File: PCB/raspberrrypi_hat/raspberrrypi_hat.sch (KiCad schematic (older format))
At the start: 18 parts, among them J1 40HAT, J2 CONN_02X02, J3 CONN_01X02, Q1 DMG2305UX, Q2 DMMT5401, U1 CAT24C32

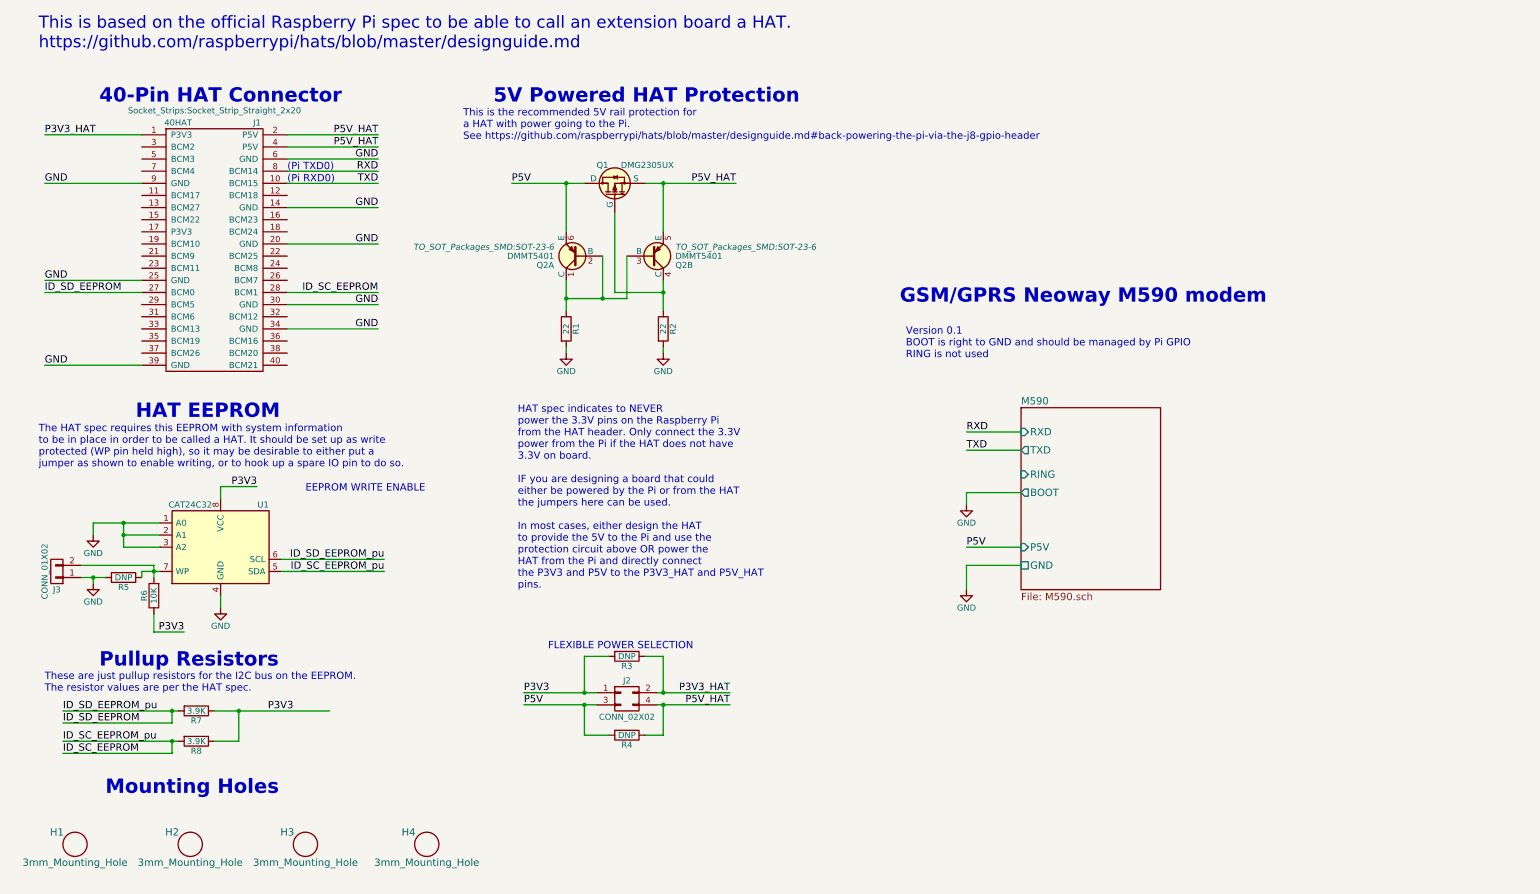
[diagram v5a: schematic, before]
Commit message: PCB: Change RPi header + add Micro SIM socket. Starting placement
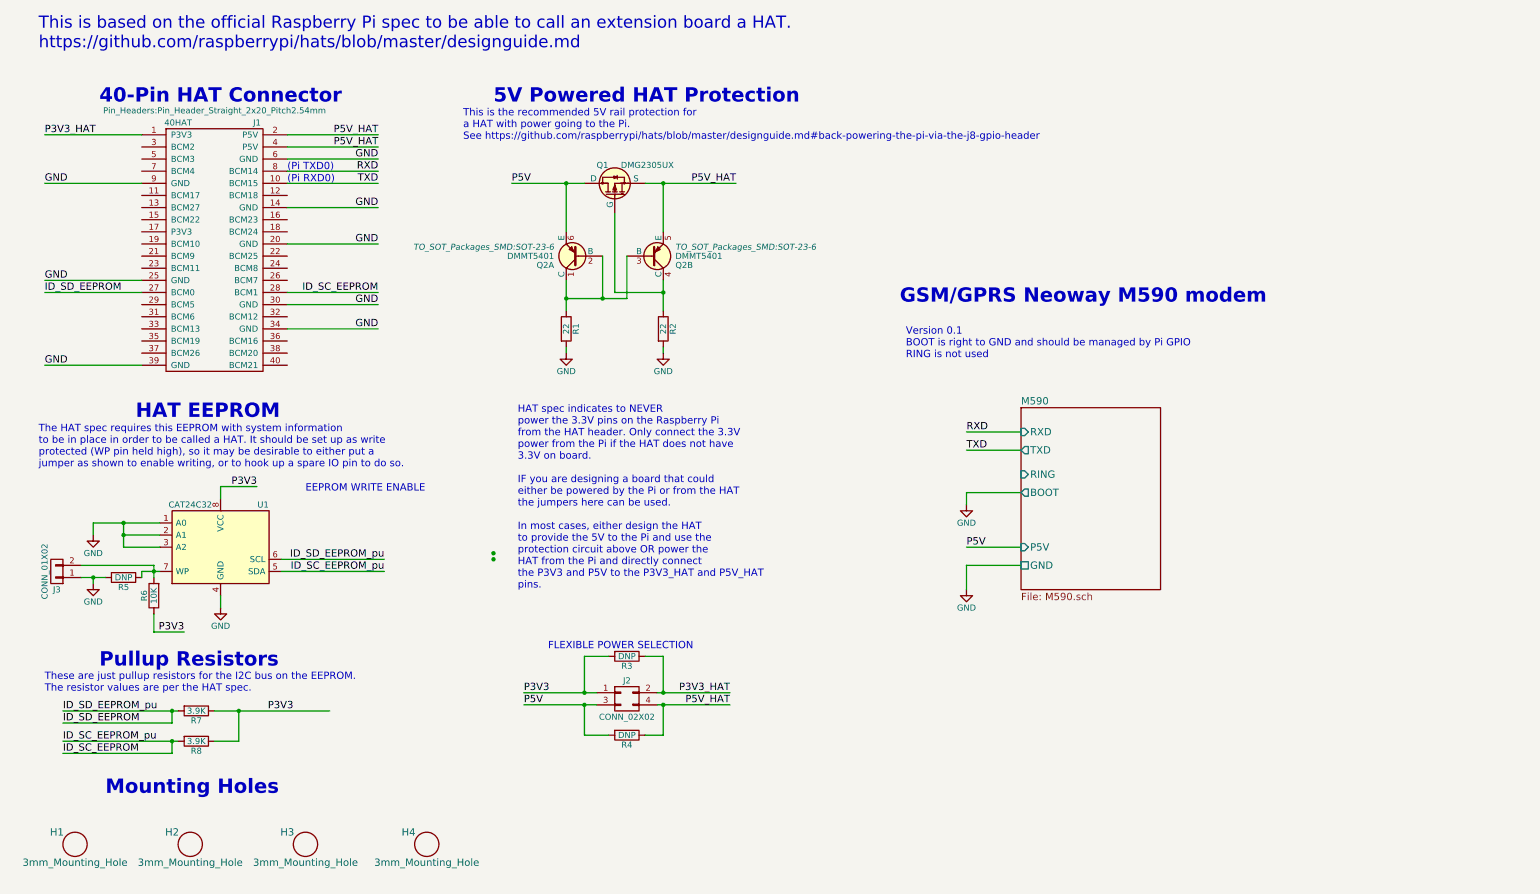
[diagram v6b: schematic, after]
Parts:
- J1: footprint Socket_Strips:Socket_Strip_Straight_2x20 -> Pin_Headers:Pin_Header_Straight_2x20_Pitch2.54mm
- J2: footprint Pin_Headers:Pin_Header_Straight_2x02 -> Pin_Headers:Pin_Header_Straight_2x02_Pitch2.54mm
- J3: footprint Pin_Headers:Pin_Header_Straight_1x02 -> Pin_Headers:Pin_Header_Straight_1x02_Pitch2.54mm
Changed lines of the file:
@@
 F 0 "J1" H 2450 1700 50  0000 C CNN
 F 1 "40HAT" H 1800 1700 50  0000 C CNN
-F 2 "Socket_Strips:Socket_Strip_Straight_2x20" H 2100 1800 50  0000 C CNN
+F 2 "Pin_Headers:Pin_Header_Straight_2x20_Pitch2.54mm" H 2100 1800 50  0000 C CNN
 F 3 "" H 1400 1600 50  0000 C CNN
 	1    2100 1600
@@
 F 0 "J2" H 5500 6400 50  0000 C CNN
 F 1 "CONN_02X02" H 5500 6100 50  0000 C CNN
-F 2 "Pin_Headers:Pin_Header_Straight_2x02" H 5500 5050 50  0001 C CNN
+F 2 "Pin_Headers:Pin_Header_Straight_2x02_Pitch2.54mm" H 5500 5050 50  0001 C CNN
 F 3 "" H 5500 5050 50  0000 C CNN
 	1    5500 6250
@@
 P5V
 Wire Wire Line
-	4650 6200 5150 6200
-Wire Wire Line
-	5150 6200 5250 6200
-Wire Wire Line
-	4650 6300 5150 6300
-Wire Wire Line
-	5150 6300 5250 6300
+	4650 6200 5250 6200
+Wire Wire Line
+	4650 6300 5250 6300
 Text Label 6350 6200 2    60   ~ 0
 P3V3_HAT
@@
 P5V_HAT
 Wire Wire Line
-	5750 6200 5800 6200
-Wire Wire Line
-	5800 6200 6350 6200
-Wire Wire Line
-	5750 6300 5800 6300
-Wire Wire Line
-	5800 6300 6350 6300
+	5750 6200 6350 6200
+Wire Wire Line
+	5750 6300 6350 6300
 Text Notes 4850 5850 0    60   ~ 0
 FLEXIBLE POWER SELECTION
@@
 P5V
 Wire Wire Line
-	4550 2000 5000 2000
-Wire Wire Line
-	5000 2000 5150 2000
+	4550 2000 5150 2000
 Text Notes 4400 1350 0    118  ~ 24
 5V Powered HAT Protection
@@
 $EndComp
 $Comp
-L GND #PWR1
+L GND #PWR01
 U 1 1 58E15A41
 P 5000 3400
-F 0 "#PWR1" H 5000 3150 50  0001 C CNN
+F 0 "#PWR01" H 5000 3150 50  0001 C CNN
 F 1 "GND" H 5000 3250 50  0000 C CNN
 F 2 "" H 5000 3400 50  0000 C CNN
@@
 $EndComp
 $Comp
-L GND #PWR2
+L GND #PWR02
 U 1 1 58E15A9E
 P 5800 3400
-F 0 "#PWR2" H 5800 3150 50  0001 C CNN
+F 0 "#PWR02" H 5800 3150 50  0001 C CNN
 F 1 "GND" H 5800 3250 50  0000 C CNN
 F 2 "" H 5800 3400 50  0000 C CNN
@@
 	5800 3400 5800 3350
 Wire Wire Line
-	5800 2800 5800 2900
-Wire Wire Line
-	5800 2900 5800 3050
+	5800 2800 5800 3050
 Wire Wire Line
 	5400 2250 5400 2900
@@
 Connection ~ 5800 2900
 Wire Wire Line
-	5000 2800 5000 2950
-Wire Wire Line
-	5000 2950 5000 3050
+	5000 2800 5000 3050
 Wire Wire Line
 	5300 2600 5300 2950
 Wire Wire Line
-	5000 2950 5300 2950
-Wire Wire Line
-	5300 2950 5500 2950
+	5000 2950 5500 2950
 Connection ~ 5000 2950
 Wire Wire Line
@@
 $EndComp
 Wire Wire Line
-	850  6350 1750 6350
-Wire Wire Line
-	1750 6350 1800 6350
-Wire Wire Line
-	850  6600 1750 6600
-Wire Wire Line
-	1750 6600 1800 6600
+	850  6350 1800 6350
+Wire Wire Line
+	850  6600 1800 6600
 Wire Wire Line
 	1750 6450 850  6450
@@
 Connection ~ 1750 6350
 Wire Wire Line
-	2100 6350 2300 6350
-Wire Wire Line
-	2300 6350 3050 6350
+	2100 6350 3050 6350
 Wire Wire Line
 	2300 6600 2100 6600
@@
 F 0 "J3" H 800 5350 50  0000 C CNN
 F 1 "CONN_01X02" V 900 5200 50  0000 C CNN
-F 2 "Pin_Headers:Pin_Header_Straight_1x02" H 800 5200 50  0001 C CNN
+F 2 "Pin_Headers:Pin_Header_Straight_1x02_Pitch2.54mm" H 800 5200 50  0001 C CNN
 F 3 "" H 800 5200 50  0000 C CNN
 	1    800  5200
@@
 	2150 4500 2150 4600
 $Comp
-L GND #PWR4
+L GND #PWR03
 U 1 1 58E1A612
 P 1100 4900
-F 0 "#PWR4" H 1100 4650 50  0001 C CNN
+F 0 "#PWR03" H 1100 4650 50  0001 C CNN
 F 1 "GND" H 1100 4750 50  0000 C CNN
 F 2 "" H 1100 4900 50  0000 C CNN
@@
 $EndComp
 Wire Wire Line
-	1350 4800 1350 4900
-Wire Wire Line
-	1350 4900 1350 5000
-Wire Wire Line
-	1100 4800 1350 4800
-Wire Wire Line
-	1350 4800 1650 4800
+	1350 4800 1350 5000
+Wire Wire Line
+	1100 4800 1650 4800
 Wire Wire Line
 	1650 4900 1350 4900
@@
 	1350 5000 1650 5000
 $Comp
-L GND #PWR5
+L GND #PWR04
 U 1 1 58E1AF98
 P 1100 5300
-F 0 "#PWR5" H 1100 5050 50  0001 C CNN
+F 0 "#PWR04" H 1100 5050 50  0001 C CNN
 F 1 "GND" H 1100 5150 50  0000 C CNN
 F 2 "" H 1100 5300 50  0000 C CNN
@@
 This is based on the official Raspberry Pi spec to be able to call an extension board a HAT.\nhttps://github.com/raspberrypi/hats/blob/master/designguide.md
 $Comp
-L GND #PWR6
+L GND #PWR05
 U 1 1 58E3CC10
 P 2150 5500
-F 0 "#PWR6" H 2150 5250 50  0001 C CNN
+F 0 "#PWR05" H 2150 5250 50  0001 C CNN
 F 1 "GND" H 2150 5350 50  0000 C CNN
 F 2 "" H 2150 5500 50  0000 C CNN
@@
 	1600 5700 1600 5550
 Wire Wire Line
-	1500 5200 1600 5200
-Wire Wire Line
-	1600 5200 1650 5200
-Wire Wire Line
-	1600 5150 1600 5200
-Wire Wire Line
-	1600 5200 1600 5250
+	1500 5200 1650 5200
+Wire Wire Line
+	1600 5150 1600 5250
 Wire Wire Line
 	1100 4800 1100 4900
@@
 Connection ~ 1600 5200
 Wire Wire Line
-	1000 5250 1100 5250
-Wire Wire Line
-	1100 5250 1200 5250
+	1000 5250 1200 5250
 Wire Wire Line
 	1100 5300 1100 5250
@@
 	1000 5150 1600 5150
 Wire Wire Line
-	5650 2000 5800 2000
-Wire Wire Line
-	5800 2000 6400 2000
+	5650 2000 6400 2000
 Text Label 2750 6350 2    60   ~ 0
 P3V3
@@
 P5V
 $Comp
-L GND #PWR3
+L GND #PWR06
 U 1 1 5952BEE9
 P 8300 4650
-F 0 "#PWR3" H 8300 4400 50  0001 C CNN
+F 0 "#PWR06" H 8300 4400 50  0001 C CNN
 F 1 "GND" H 8300 4500 50  0000 C CNN
 F 2 "" H 8300 4650 50  0000 C CNN
@@
 	8300 5150 8300 5350
 $Comp
-L GND #PWR?
+L GND #PWR07
 U 1 1 5955690F
 P 8300 5350
-F 0 "#PWR?" H 8300 5100 50  0001 C CNN
+F 0 "#PWR07" H 8300 5100 50  0001 C CNN
 F 1 "GND" H 8300 5200 50  0000 C CNN
 F 2 "" H 8300 5350 50  0000 C CNN
@@
 Text Notes 7800 3450 0    60   ~ 0
 Version 0.1\nBOOT is right to GND and should be managed by Pi GPIO\nRING is not used
+Connection ~ 4400 5050
+Connection ~ 4400 5100
 $EndSCHEMATC
